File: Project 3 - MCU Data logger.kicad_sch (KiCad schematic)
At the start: 26 parts, among them U1 24AA02-OT, U2 24AA02-OT, U3 DS1337, U4 ATMEGA328P-AU, Y1 Crystal, Y2 Crystal

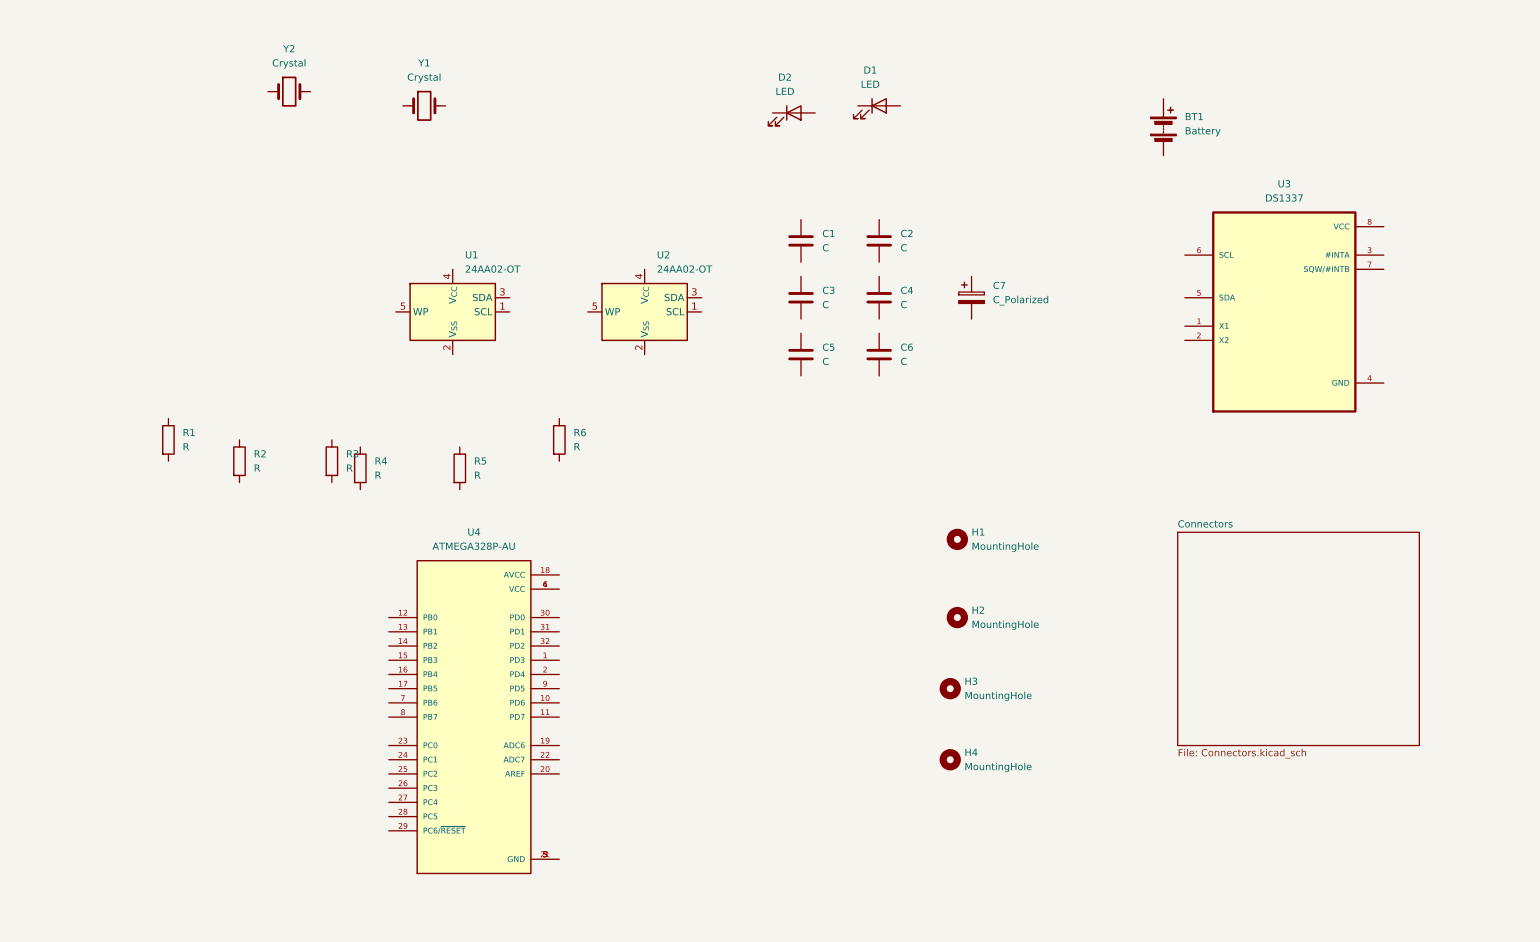
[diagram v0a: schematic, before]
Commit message: wire up timer,eeprom,mcu
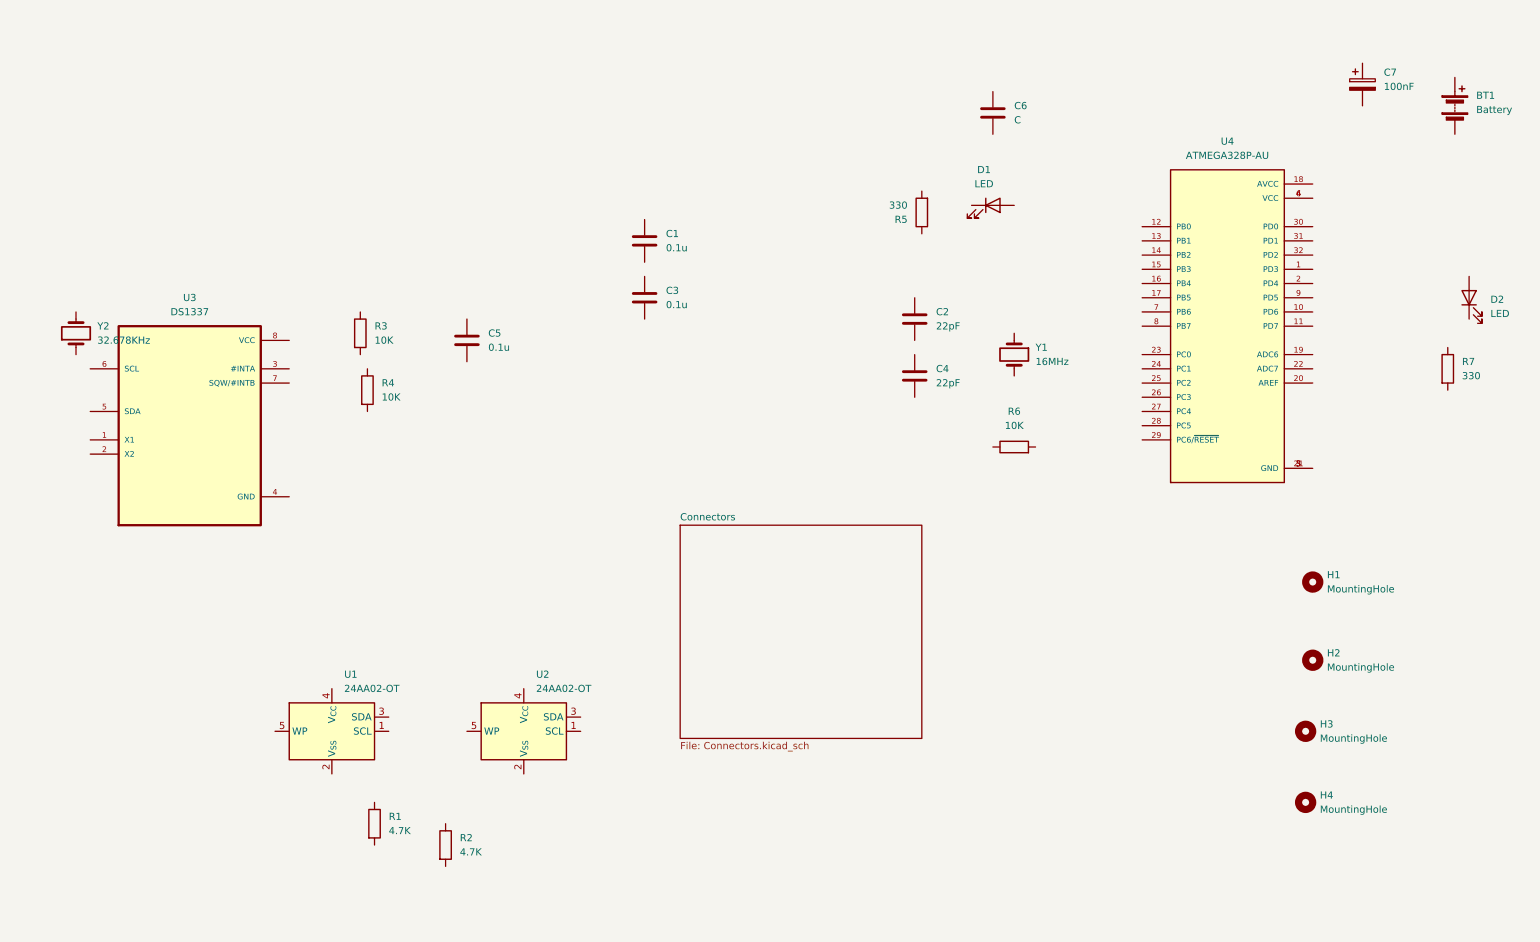
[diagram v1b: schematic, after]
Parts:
- added R7: 330, Resistor_SMD:R_0805_2012Metric, symbol Device:R
- BT1: footprint (none) -> Connector_PinSocket_2.54mm:PinSocket_1x02_P2.54mm_Vertical
- C1, C3, C5: value C -> 0.1u; footprint (none) -> Capacitor_SMD:C_0805_2012Metric
- C2, C4: value C -> 22pF; footprint (none) -> Capacitor_SMD:C_0805_2012Metric
- C6: footprint (none) -> Capacitor_SMD:C_0805_2012Metric
- C7: value C_Polarized -> 100nF; footprint (none) -> Capacitor_SMD:C_0805_2012Metric
- D1, D2: footprint (none) -> LED_SMD:LED_0805_2012Metric
- H1, H2, H3, H4: footprint (none) -> MountingHole:MountingHole_2.1mm
- R1, R2: value R -> 4.7K; footprint (none) -> Resistor_SMD:R_0805_2012Metric
- R3, R4, R6: value R -> 10K; footprint (none) -> Resistor_SMD:R_0805_2012Metric
- R5: value R -> 330; footprint (none) -> Resistor_SMD:R_0805_2012Metric
- U1, U2: footprint Package_TO_SOT_SMD:SOT-23-5 -> Package_SO:SOIC-8_5.23x5.23mm_P1.27mm
- Y1: value Crystal -> 16MHz; footprint (none) -> Crystal:Crystal_SMD_5032-2Pin_5.0x3.2mm_HandSoldering
- Y2: value Crystal -> 32.678KHz; footprint (none) -> Crystal:Crystal_SMD_5032-2Pin_5.0x3.2mm_HandSoldering
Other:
- moved on the sheet: BT1, C1, C2, C3, C4, C5, C6, C7, D1, D2, H1, H2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

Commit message: added wiring for second sheet
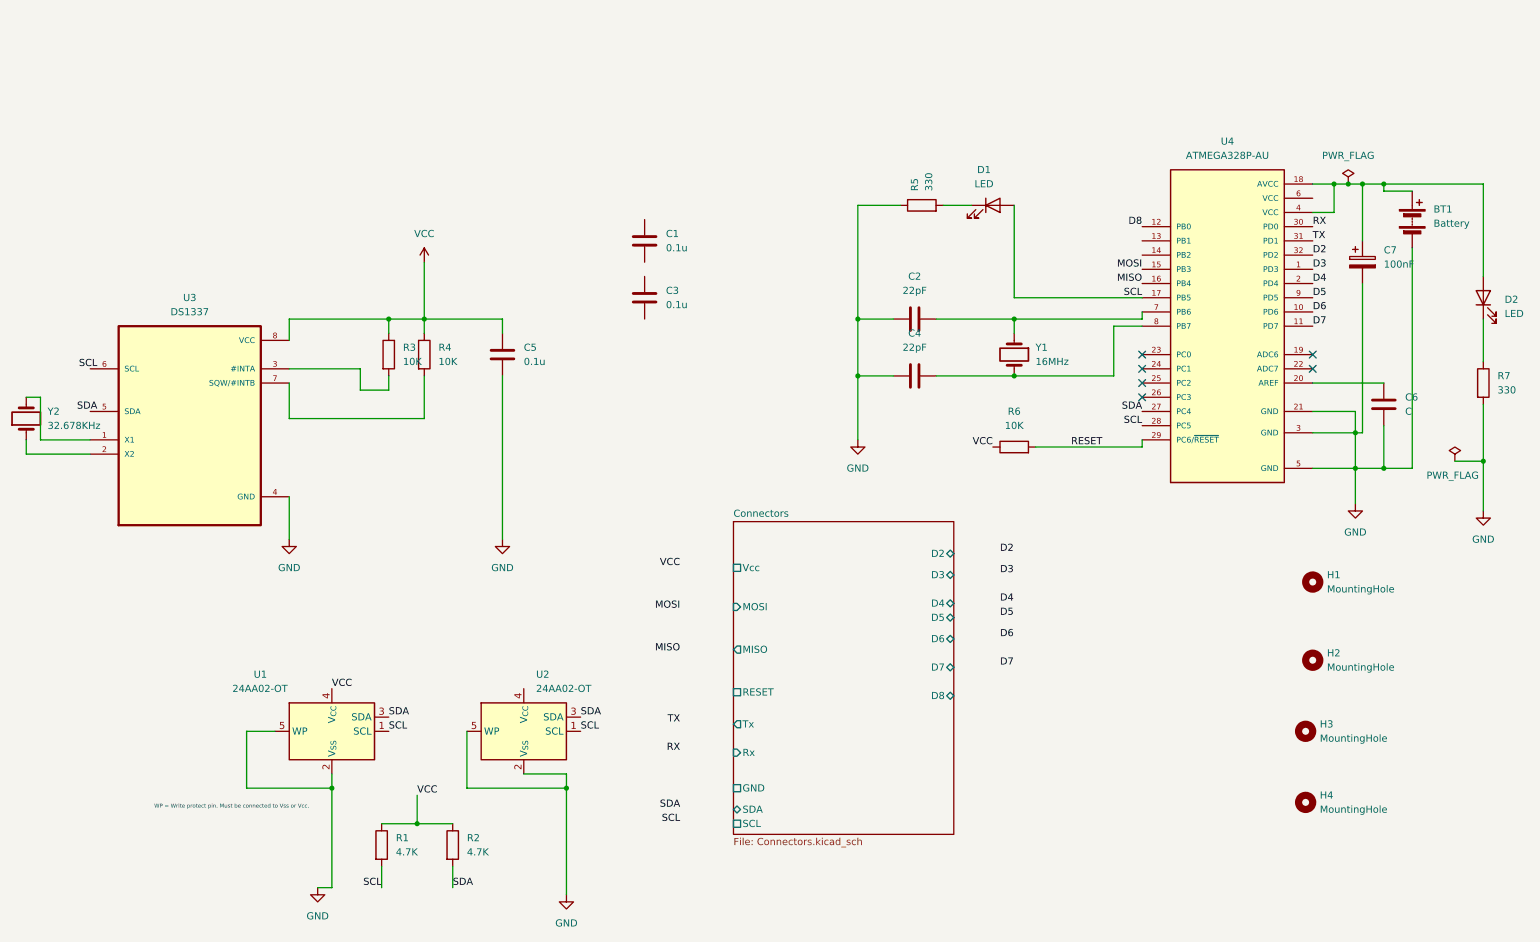
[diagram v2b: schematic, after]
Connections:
- net at R7.1: now also D2.1 (K)
- net GND: now reaches R7.2
- net GND: now also BT1.2 (-), C2.1, C4.1, C5.2, C6.1, C7.2, R5.1, U1.2 (V_{SS}), U1.5 (WP), U2.2 (V_{SS}), U2.5 (WP), U3.4 (GND), U4.21 (GND), U4.3 (GND), U4.5 (GND)
- net at U3.1 (X1): now also Y2.2
- net at U3.2 (X2): now also Y2.1
- net at U3.3 (#INTA): now also R3.2
- net at U3.7 (SQW/#INTB): now also R4.2
- net VCC: now reaches U3.8 (VCC)
- net VCC: now also C5.1, R1.1, R2.1, R3.1, R4.1, R6.1, U1.4 (V_{CC})
- net D3: now reaches U4.1 (PD3)
- net D6: now reaches U4.10 (PD6)
- net D7: now reaches U4.11 (PD7)
- net D8: now reaches U4.12 (PB0)
- net MOSI: now reaches U4.15 (PB3)
- net MISO: now reaches U4.16 (PB4)
- net SCL: now reaches U4.17 (PB5)
- net SCL: now also D1.2 (A), R1.2, U1.1 (SCL), U2.1 (SCL), U4.28 (PC5)
- net at U4.18 (AVCC): now also BT1.1 (+), C7.1, D2.2 (A), U4.4 (VCC)
- net D4: now reaches U4.2 (PD4)
- net at U4.20 (AREF): now also C6.2
- net SDA: now reaches U4.27 (PC4)
- net SDA: now also R2.2, U1.3 (SDA), U2.3 (SDA)
- net RESET: now reaches U4.29 (PC6/~{RESET})
- net RESET: now also R6.2
- net RX: now reaches U4.30 (PD0)
- net TX: now reaches U4.31 (PD1)
- net D2: now reaches U4.32 (PD2)
- net at U4.6 (VCC): no longer U4.4 (VCC)
- net at U4.7 (PB6): now also C2.2, Y1.1
- net at U4.8 (PB7): now also C4.2, Y1.2
- net D5: now reaches U4.9 (PD5)
- net at R5.2: now also D1.1 (K)
- no-connect marks 0 -> 6
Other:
- sheet Connectors ports: added D2, D3, D4, D5, D6, D7, D8, GND, MISO, MOSI, RESET, Rx, SCL, SDA, Tx, Vcc; removed none
- note added: "WP = Write protect pin. Must be connected to Vss or Vcc."
- moved on the sheet: BT1, C2, C4, C5, C6, C7, D2, R1, R2, R3, R4, R5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

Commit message: add comments and netclass for power
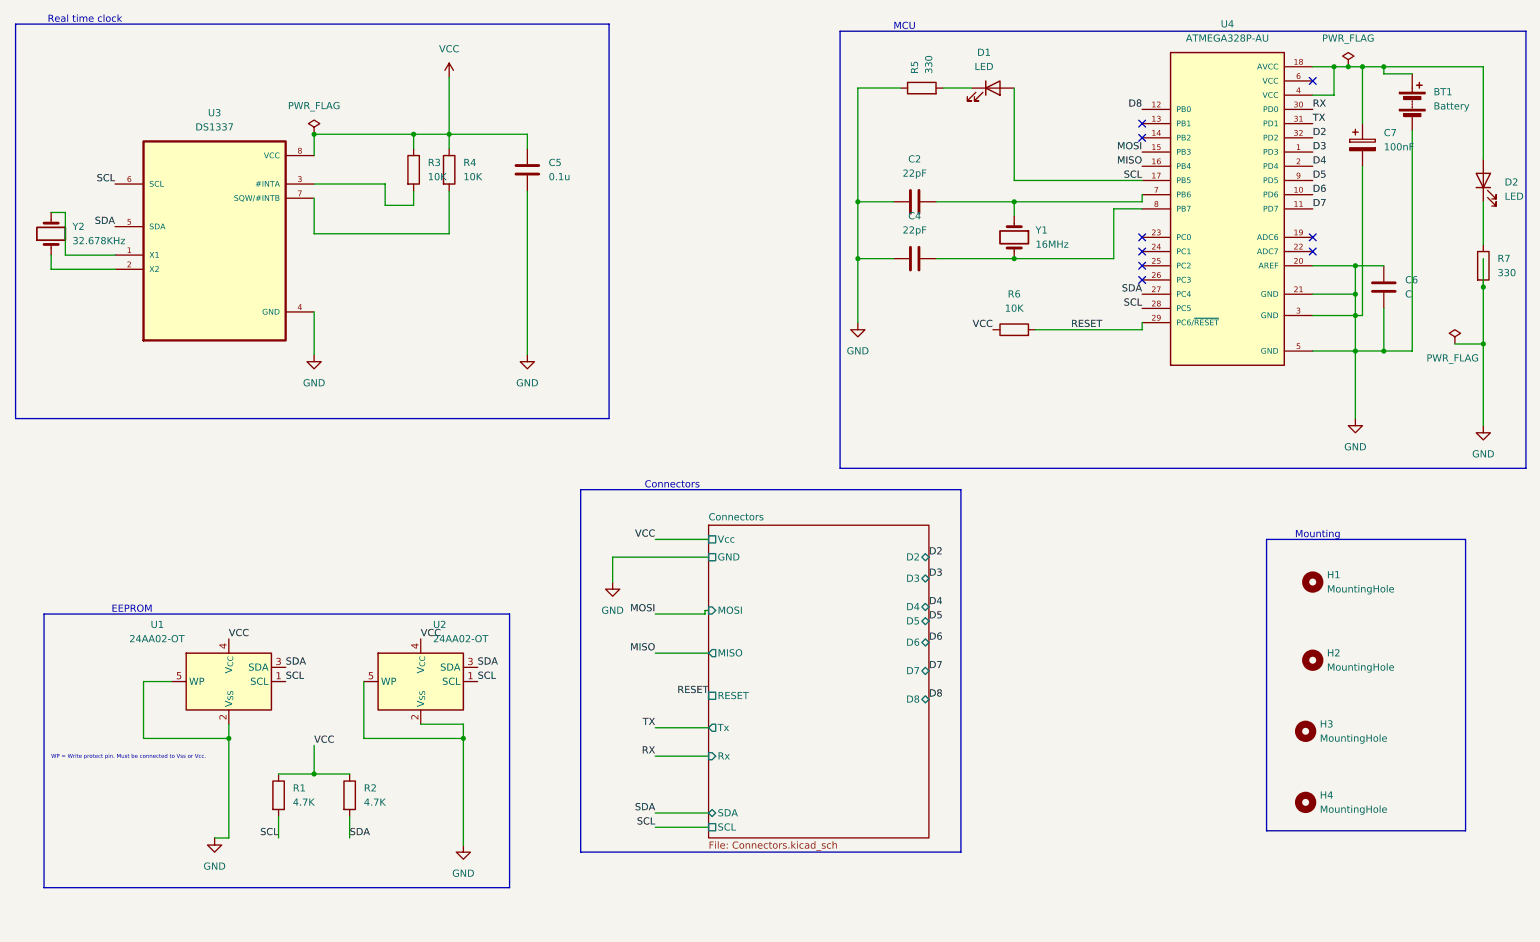
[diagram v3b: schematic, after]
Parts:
- removed C1, C3: 0.1u, Capacitor_SMD:C_0805_2012Metric, symbol Device:C
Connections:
- net GND: now also C6.2, U4.20 (AREF)
- net SCL: now also U3.6 (SCL)
- net SDA: now also U3.5 (SDA)
- net VCC: now also U2.4 (V_{CC})
- no-connect marks 6 -> 9
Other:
- note added: "Connectors"
- note added: "EEPROM"
- note added: "MCU"
- note added: "Mounting"
- note added: "Real time clock"
- moved on the sheet: BT1, C2, C4, C5, C6, C7, D1, D2, R1, R2, R3, R4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
